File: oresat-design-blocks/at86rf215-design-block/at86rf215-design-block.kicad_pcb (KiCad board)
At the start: 4 copper layers, 61.3 x 44.1 mm, 80 parts, among them J1 SMA, J10 Conn_01x08, J11 Conn_01x05, J12 Conn_01x08, J2 USB4105-GF-A, J3 Conn_01x06, J4 SMA, J6 Conn_01x06, J7 SMA, J8 SMA, J9 Screw_Terminal_01x02, SW1 RESET, U1 AT86RF215, U2 LP2985AIM5-1.8_NOPB, U3 2450FB15A050E, U5 QPC1022, U7 NCS2-62+, X1 TXETALSANF-26.000000

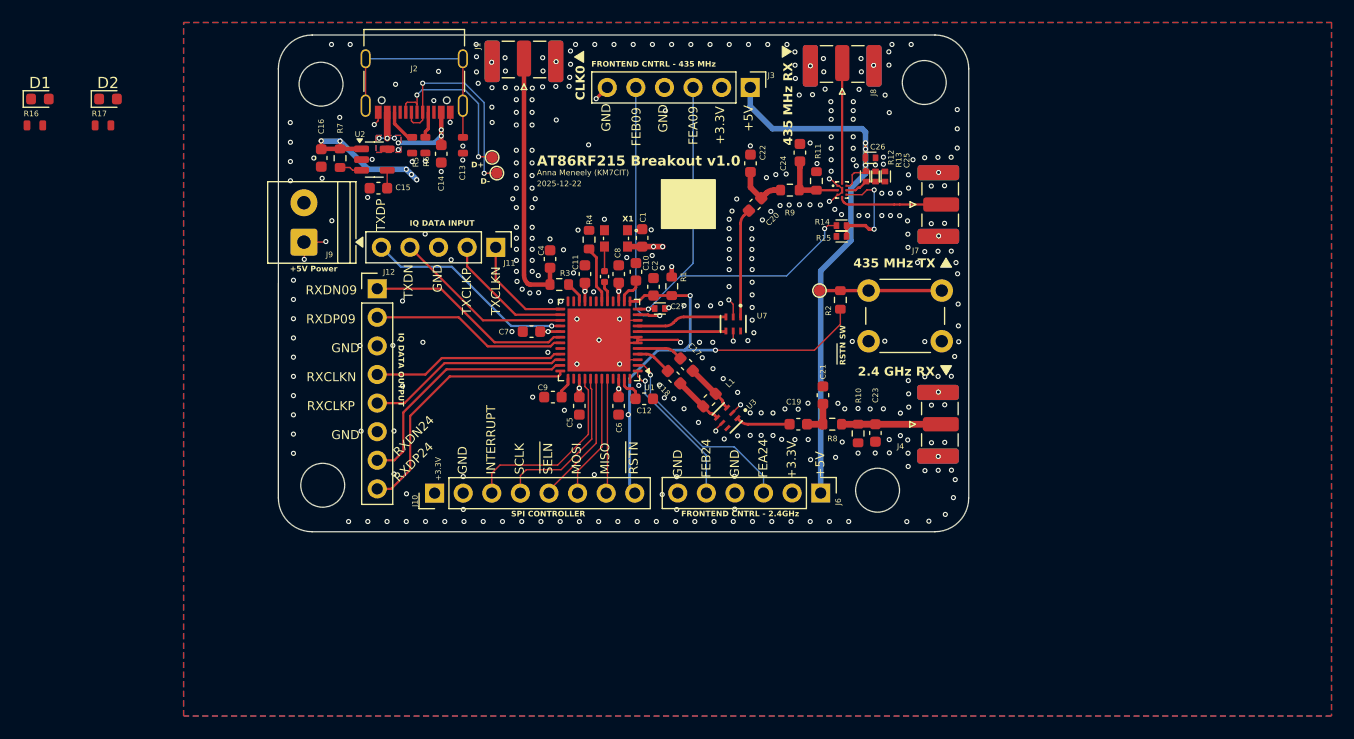
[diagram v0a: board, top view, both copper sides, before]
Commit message: swapped 0402 to 0603 and fixed layout, routed LEDs, fixed SMAs,  and fixed silkscreen
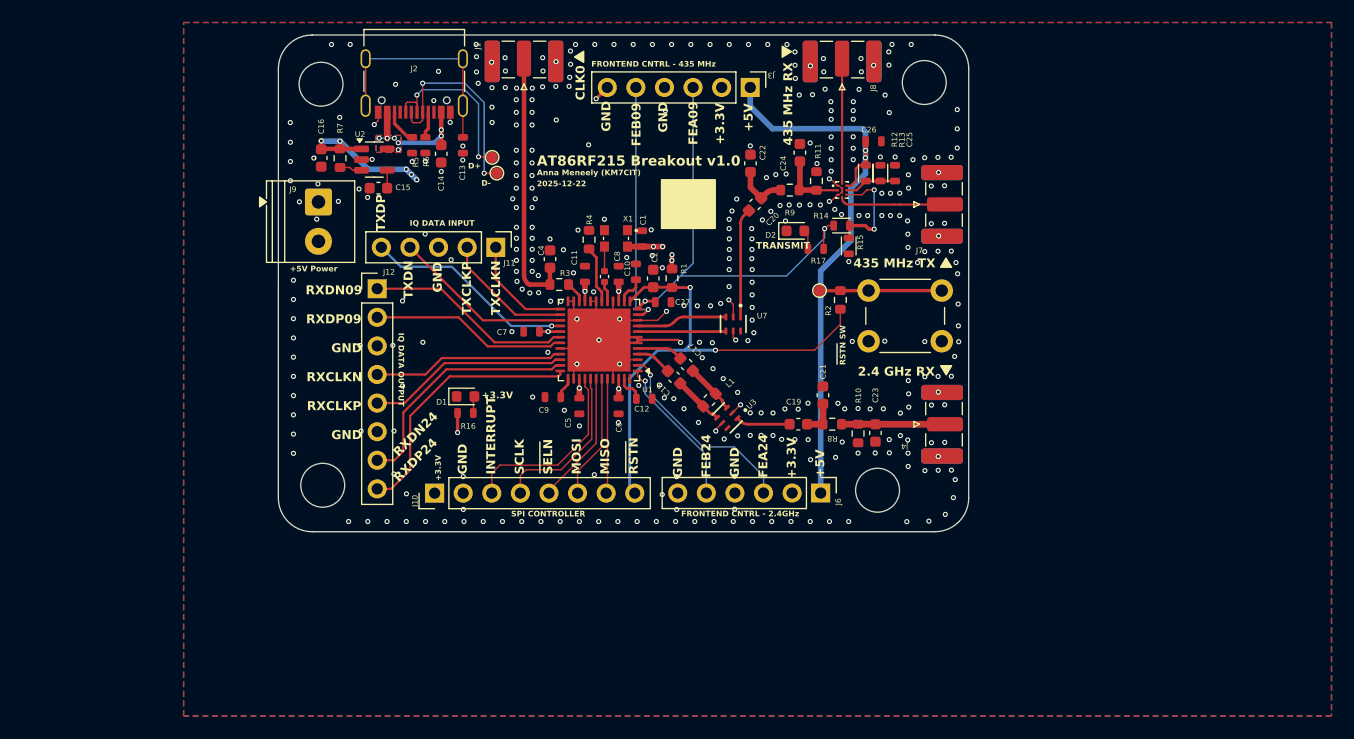
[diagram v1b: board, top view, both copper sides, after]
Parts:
- C1: footprint Capacitor_SMD:C_0603_1608Metric -> oresat-passives:0603-C-NOSILK
- C10, C11, C12, C5, C6, C7, C8, C9: value 100 nF -> 100n; footprint Capacitor_SMD:C_0603_1608Metric -> oresat-passives:0603-C-NOSILK
- C25, C26, C27: footprint oresat-passives:0402-C -> oresat-passives:0603-C-NOSILK
- R12, R13, R14, R15: footprint oresat-passives:0402-C -> oresat-passives:0603-C
- moved R17 64.3 mm to (138.6, 73.3), turned to 180 degrees
- moved D2 62.2 mm to (136.8, 71.7)
- moved D1 46.1 mm to (107.5, 86.4)
- moved R16 46.0 mm to (107.5, 87.9)
- moved J9 3.80 mm to (94.4, 69.2), turned to -90 degrees
- moved C26 1.49 mm to (143.7, 63.8)
- moved R15 1.06 mm to (141.5, 73.1), turned to -90 degrees
- moved C25 0.95 mm to (145.6, 66.6)
- moved C2 0.74 mm to (124.1, 76.0)
- moved R1 0.71 mm to (125.8, 75.9)
- moved C27 0.64 mm to (125.0, 78.0)
- moved R13 0.53 mm to (144.3, 66.6)
- moved J8 0.39 mm to (140.9, 56.4)
- moved J4 0.37 mm to (150.1, 88.9)
- moved J7 0.34 mm to (150.1, 69.4)
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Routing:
- net GND: track 35.1 -> 51.3 mm, vias 359 -> 360
- net +3.3V: track 129.8 -> 123.2 mm, vias 13 -> 15
- net FEB09: track 24.0 -> 21.9 mm
- net Net-(D2-A): track 0.00 -> 1.73 mm
- net Net-(D1-A): track 0.00 -> 1.51 mm
- net FEA09: track 39.6 -> 41.0 mm
- net ~{RSTN}: track 43.1 -> 44.1 mm
- net +5V: track 110.7 -> 109.7 mm, vias 10 -> 9
- net Net-(U5-EN): track 3.72 -> 4.64 mm
- net Net-(J8-In): track 10.7 -> 11.5 mm
- net Net-(J7-In): track 8.81 -> 9.55 mm
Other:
- board text added: "TRANSMIT"

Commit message: Final polish on AT86 board
Changed differential lines to 100 ohms, uncovered all RF traces with solder mask, switch all caps and resistors to common footprint, added most BOM parts, moved RF components to not add stubs, fixed DRC violations and cleaned up silk screen.
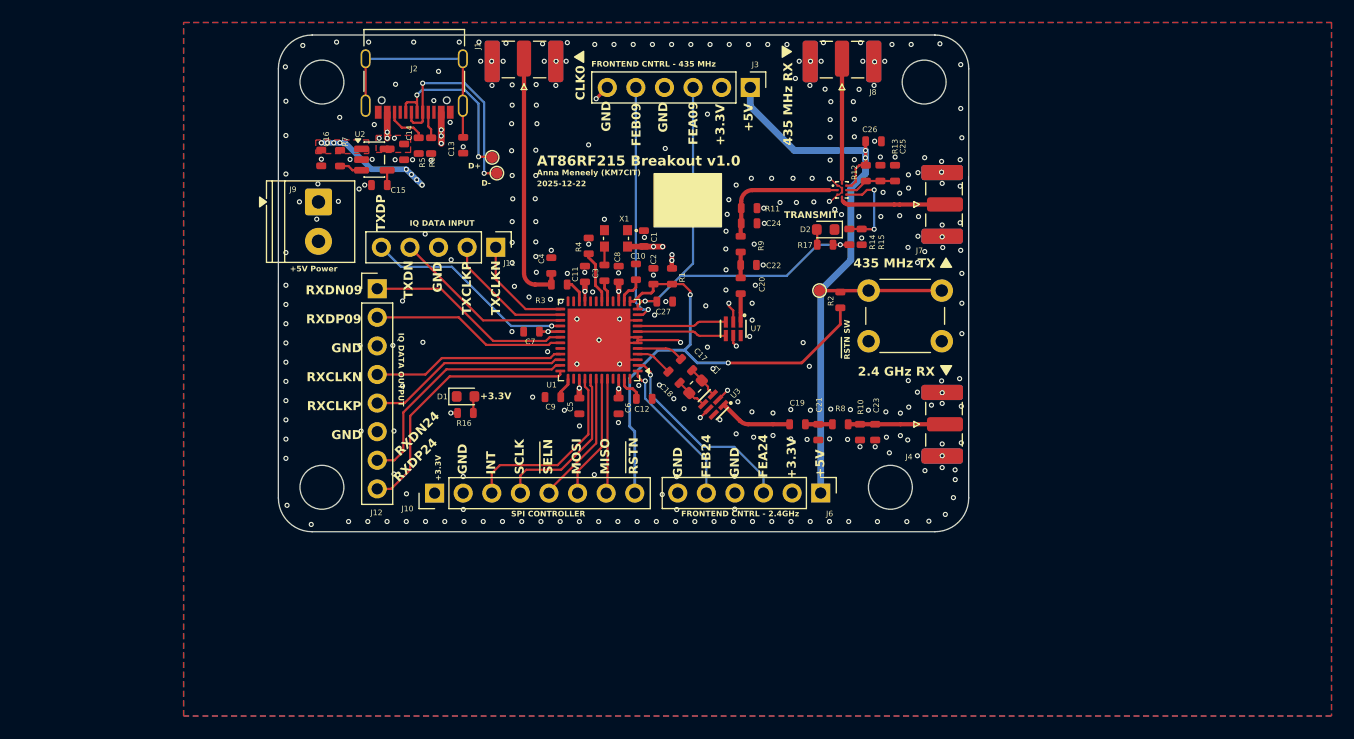
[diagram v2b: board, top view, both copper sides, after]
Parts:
- C14, C15, C16, C17, C18, C19, C2, C20, C21, C22, C23, C24, C4: footprint Capacitor_SMD:C_0603_1608Metric -> oresat-passives:0603-C-NOSILK
- C3: footprint Capacitor_SMD:C_0402_1005Metric -> oresat-passives:0603-C-NOSILK
- R1, R10, R11, R3, R4, R7, R8, R9: footprint Resistor_SMD:R_0603_1608Metric -> oresat-passives:0603-C-NOSILK
- R12, R13, R14, R15: footprint oresat-passives:0603-C -> oresat-passives:0603-C-NOSILK
- R2: value 39 -> 220; footprint Resistor_SMD:R_0603_1608Metric -> oresat-passives:0603-C-NOSILK
- moved C22 9.03 mm to (132.6, 74.8), turned to 0 degrees
- moved C24 7.73 mm to (132.7, 71.0), turned to 0 degrees
- moved C20 7.34 mm to (131.9, 76.6), turned to -90 degrees
- moved R9 6.49 mm to (131.9, 72.9), turned to 90 degrees
- moved R11 6.45 mm to (132.7, 69.7), turned to 0 degrees
- moved TP5 3.96 mm to (131.9, 78.2)
- moved C21 3.31 mm to (138.8, 89.6), turned to -90 degrees
- moved C14 3.30 mm to (102.0, 64.7)
- moved D2 2.69 mm to (139.4, 71.6), turned to 180 degrees
- moved L1 1.71 mm to (127.9, 85.6)
- moved U3 1.71 mm to (129.5, 87.2)
- moved R15 1.41 mm to (142.7, 72.2)
- moved R14 1.21 mm to (141.6, 72.2), turned to 90 degrees
- moved H3 1.17 mm to (145.2, 94.5)
- moved R17 0.91 mm to (139.4, 73.0)
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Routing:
- net +3.3V: track 123.2 -> 23.6 mm, vias 15 -> 18
- net GND: track 51.3 -> 33.1 mm, vias 360 -> 303
- net +5V: track 109.7 -> 101.1 mm
- net Net-(C20-Pad2): track 9.71 -> 2.53 mm
- net Net-(U5-RF_COM): track 5.97 -> 12.2 mm
- net Net-(C20-Pad1): track 4.70 -> 2.25 mm
- net Net-(C19-Pad2): track 4.82 -> 6.55 mm
- net Net-(C17-Pad1): track 4.53 -> 2.85 mm
- net Net-(C18-Pad2): track 4.51 -> 2.89 mm
- net ~{RSTN}: track 44.1 -> 45.4 mm
- net Net-(U5-CTRL): track 9.59 -> 8.34 mm
- net FEA09: track 41.0 -> 40.1 mm
- net Net-(C19-Pad1): track 3.22 -> 2.42 mm
- net Net-(J2-D+-PadA6): track 16.3 -> 15.5 mm
- net Net-(J2-CC2): track 3.08 -> 3.76 mm
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- added copper zone on F.Cu, net +3.3V
- removed copper zone on B.Cu, net +5V
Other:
- board text added: "INT"
- board text removed: "INTERRUPT"

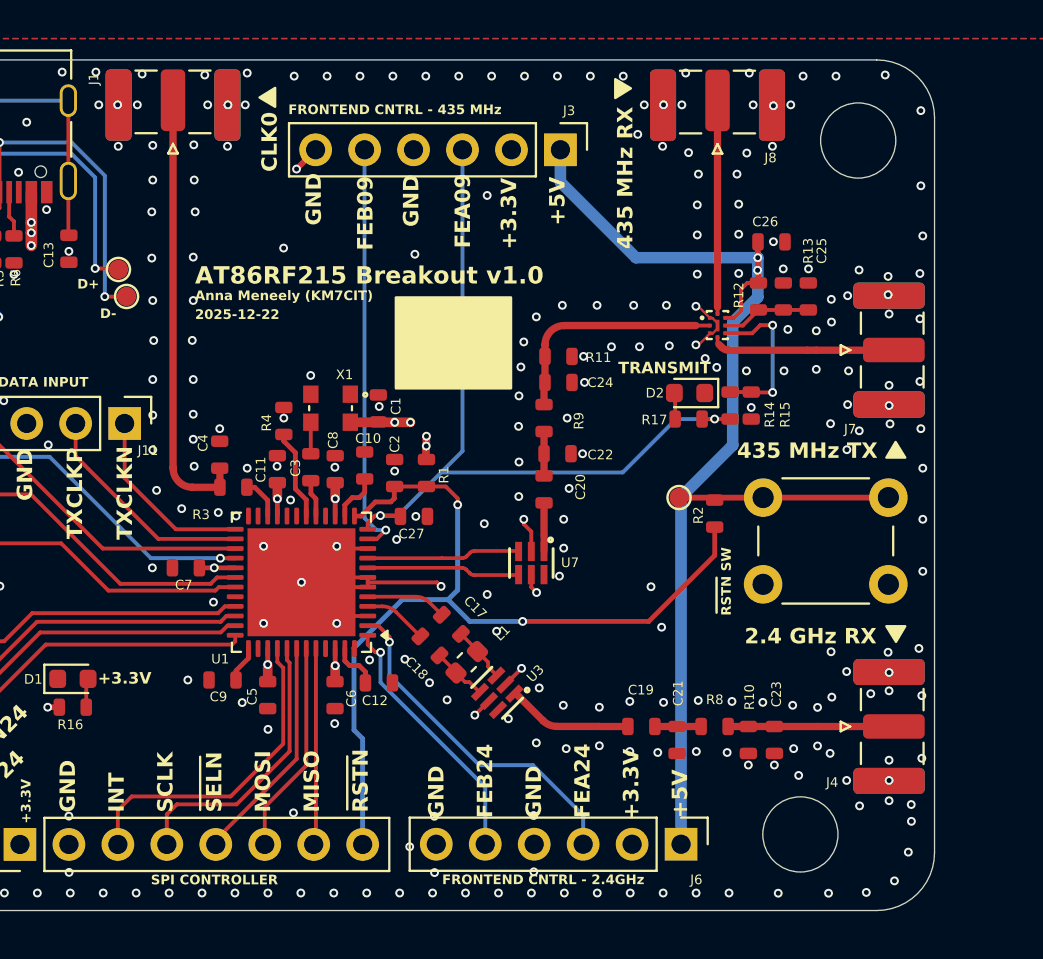
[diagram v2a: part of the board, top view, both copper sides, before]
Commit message: Last minute fixes and polishing.
Added capacitor and LED BOM part numbers. Fixed balun footprint and layout; had the wrong idea of how to lay it out. Now more closely matches the evaluation board. Also everything now 50 ohms, even the diff pairs. Fixed solder mask over RF. Better silkscreen too.
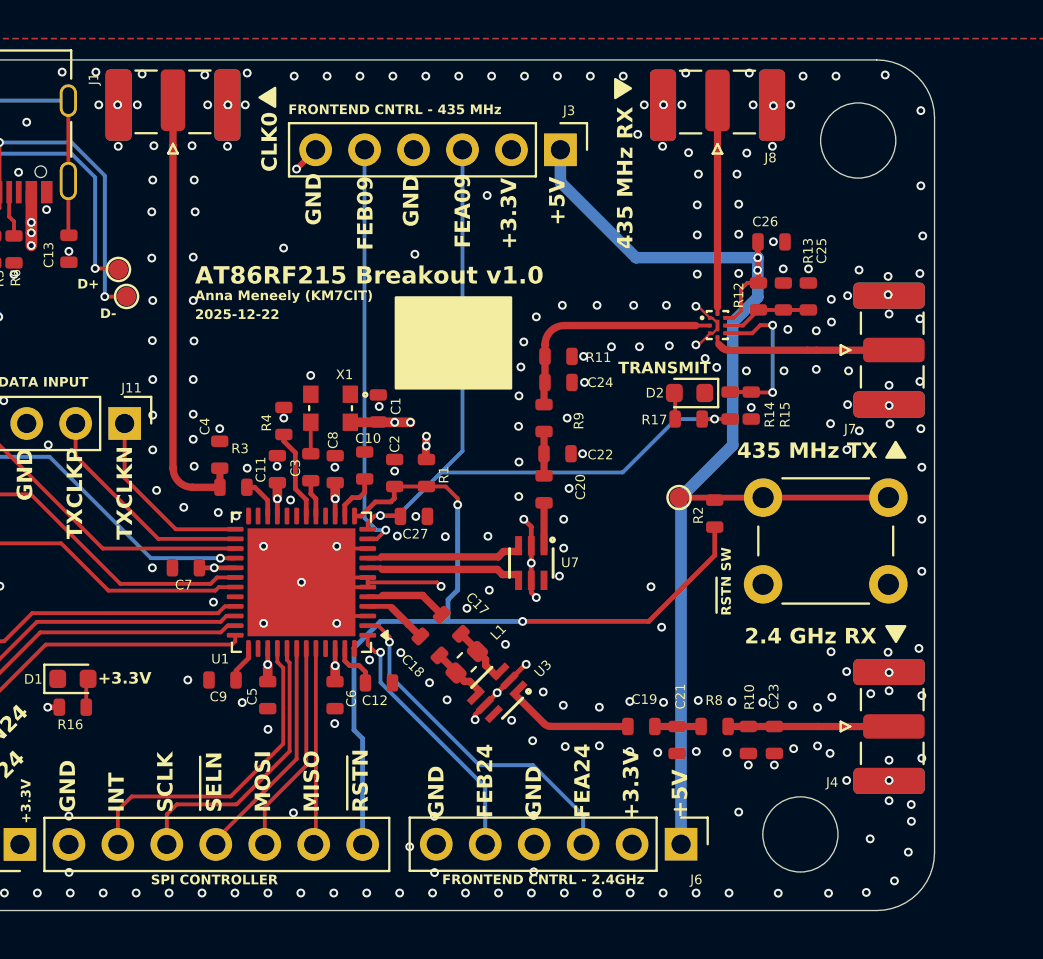
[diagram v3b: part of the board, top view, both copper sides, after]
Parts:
- moved TP10 10.1 mm to (112.7, 58.8)
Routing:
- net GND: track 33.1 -> 36.9 mm, vias 303 -> 307

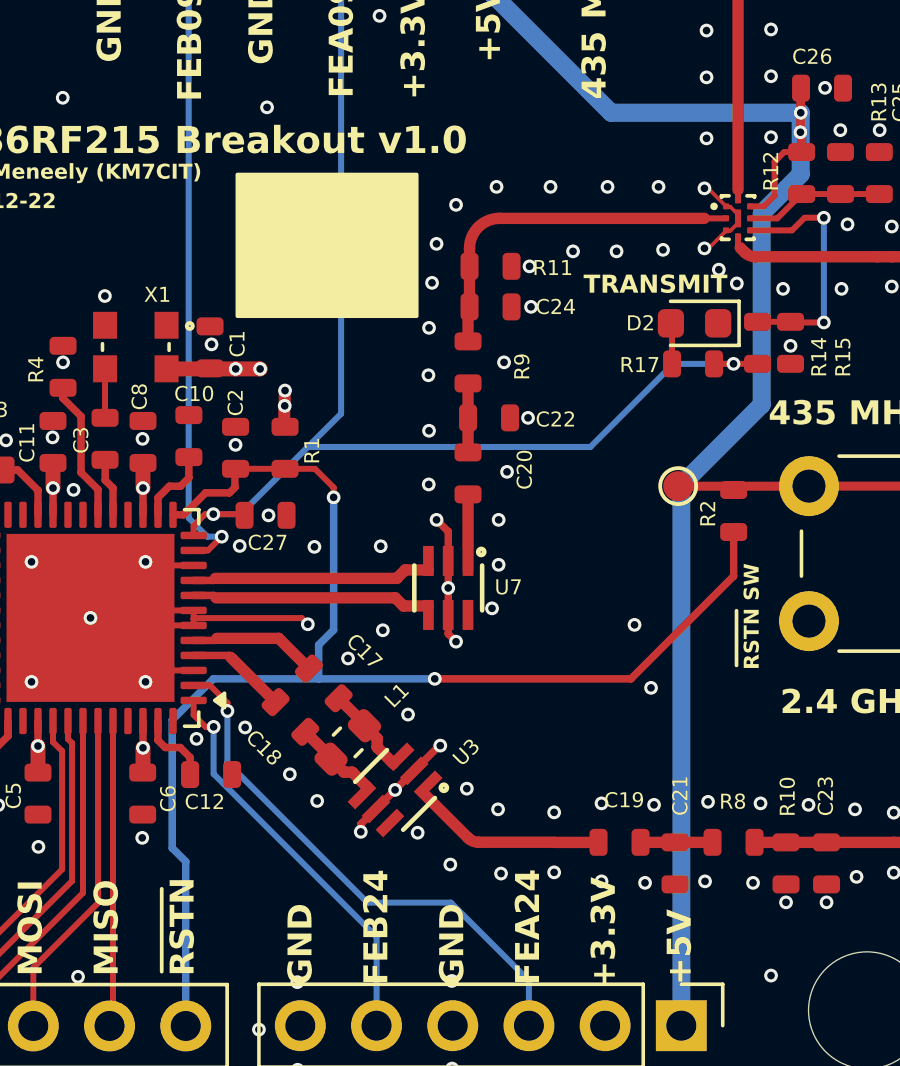
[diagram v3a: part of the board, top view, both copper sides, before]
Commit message: fixed the balun pin assignments, added clarifying notes on schematic, rerouted the baluns on the physical board
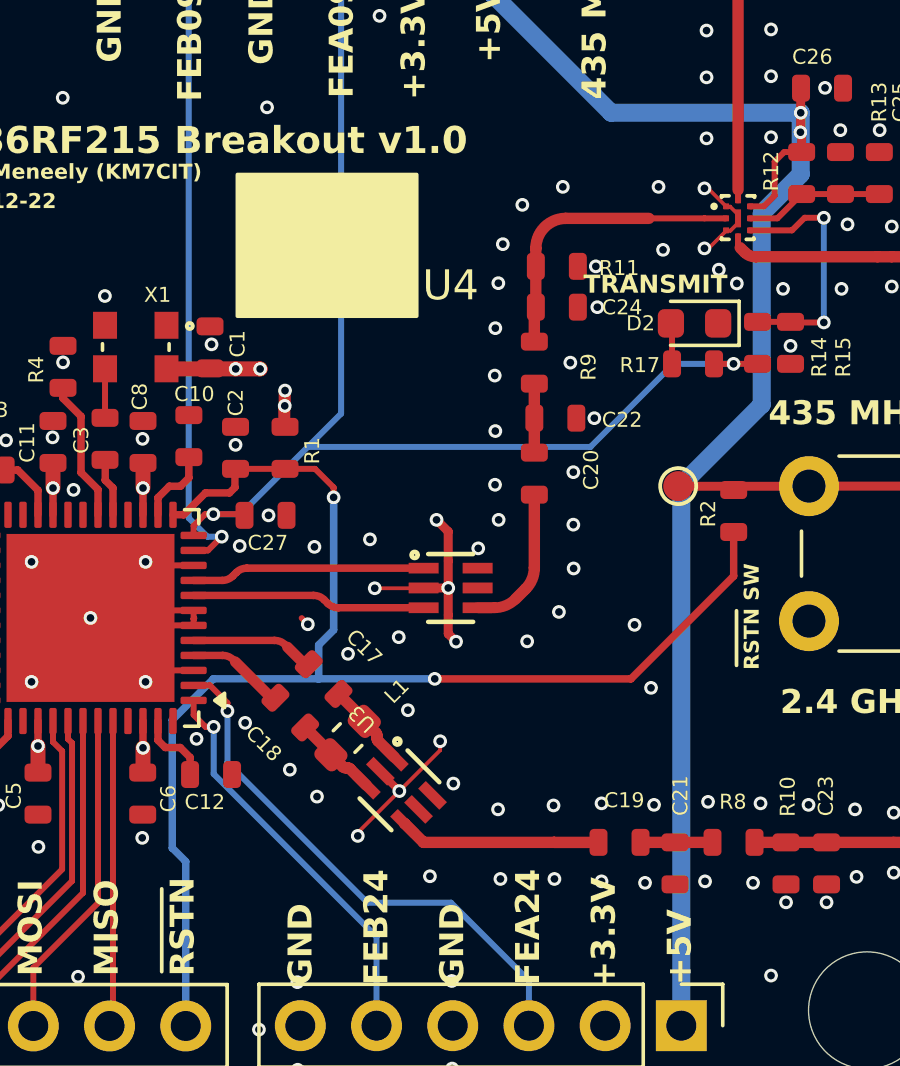
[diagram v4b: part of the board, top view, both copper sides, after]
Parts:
- removed U7: NCS2-62+, oresat-passives:2450FB15A050E_JOT
- added U4: NCS2-62+, oresat-passives:2450FB15A050E_JOT, F.Cu at (131.3, 80.4)
- C20: value 15p -> 0.8p
- moved C20 2.21 mm to (134.1, 76.6)
- moved C22 2.21 mm to (134.8, 74.8)
- moved C24 2.21 mm to (134.9, 71.1)
- moved R9 2.21 mm to (134.1, 72.9)
- moved TP5 2.21 mm to (134.1, 78.2)
- moved R11 2.21 mm to (134.9, 69.7)
- moved U3 0.15 mm to (129.6, 87.2), turned to -45 degrees
- moved C17 0.15 mm to (127.1, 83.5)
- moved C18 0.15 mm to (126.0, 84.6)
- moved L1 0.15 mm to (127.9, 85.4)
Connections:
- U3 pad 1: Net-(C19-Pad2) -> Net-(C17-Pad1)
- U3 pad 3: Net-(C17-Pad1) -> Net-(C18-Pad2)
- U3 pad 4: Net-(C18-Pad2) -> Net-(C19-Pad2)
- U3 pad 5: GND -> unconnected-(U3-NC-Pad5)
- U3 pad 6: unconnected-(U3-NC-Pad6) -> GND
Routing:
- net Net-(C20-Pad2): track 2.53 -> 5.02 mm
- net Net-(U5-RF_COM): track 12.2 -> 9.99 mm
- net GND: track 36.9 -> 36.5 mm, vias 307 -> 306
